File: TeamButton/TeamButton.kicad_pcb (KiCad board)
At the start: 2 copper layers, 79.9 x 70 mm, 5 parts, among them J1 RJ45, SW1 10T85 Microswitch, SW2 10T85 Microswitch

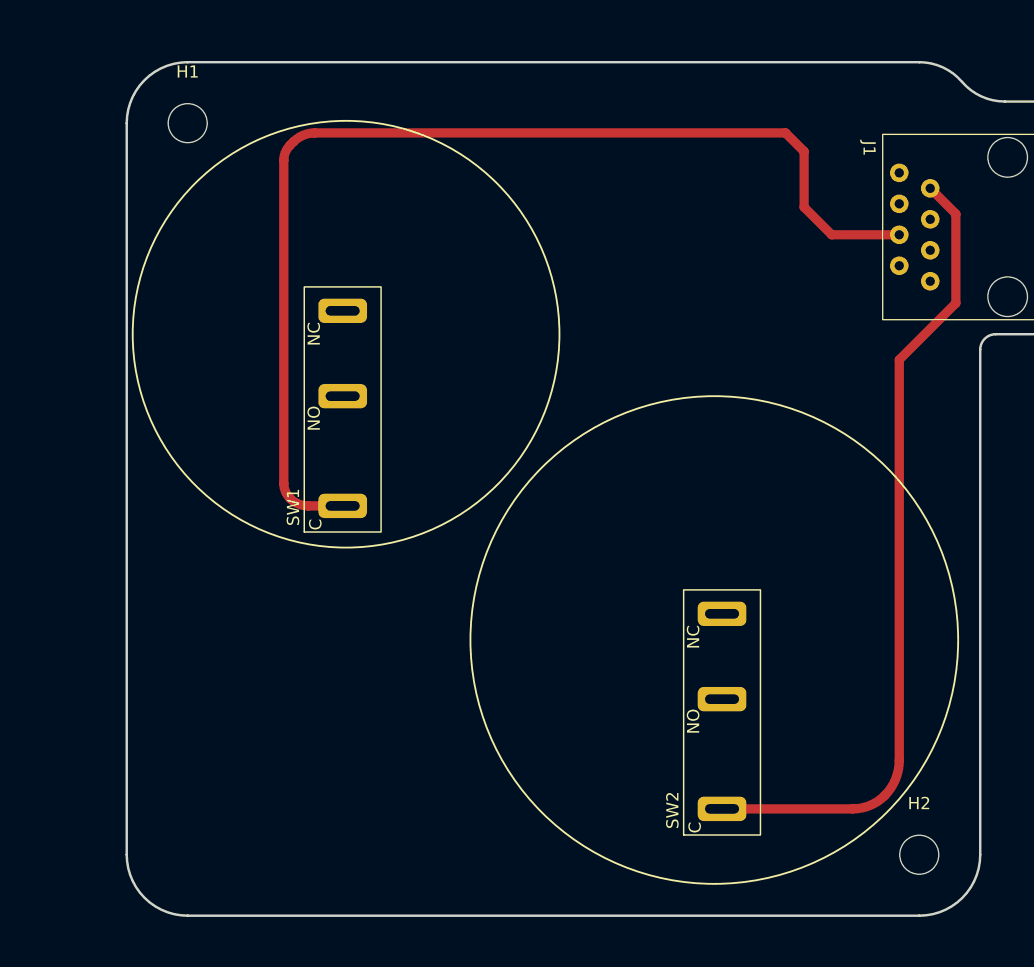
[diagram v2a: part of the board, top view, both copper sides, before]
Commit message: Added gay notations.
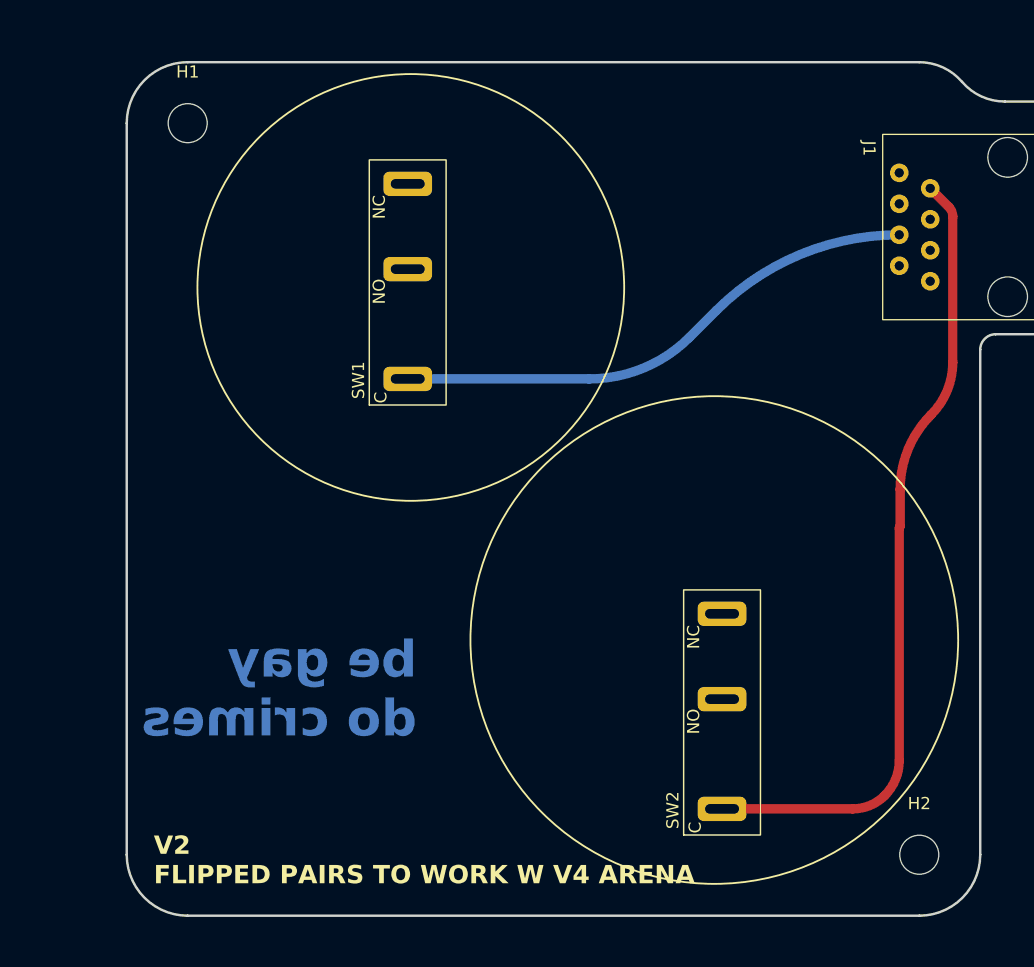
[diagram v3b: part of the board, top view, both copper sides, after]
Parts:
- moved SW1 11.7 mm to (94.9, 73.1)
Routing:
- net Net-(SW1-C): track 90.1 -> 43.6 mm
- net Net-(SW2-C): track 66.5 -> 65.5 mm
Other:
- board text added: "be gay do crimes"

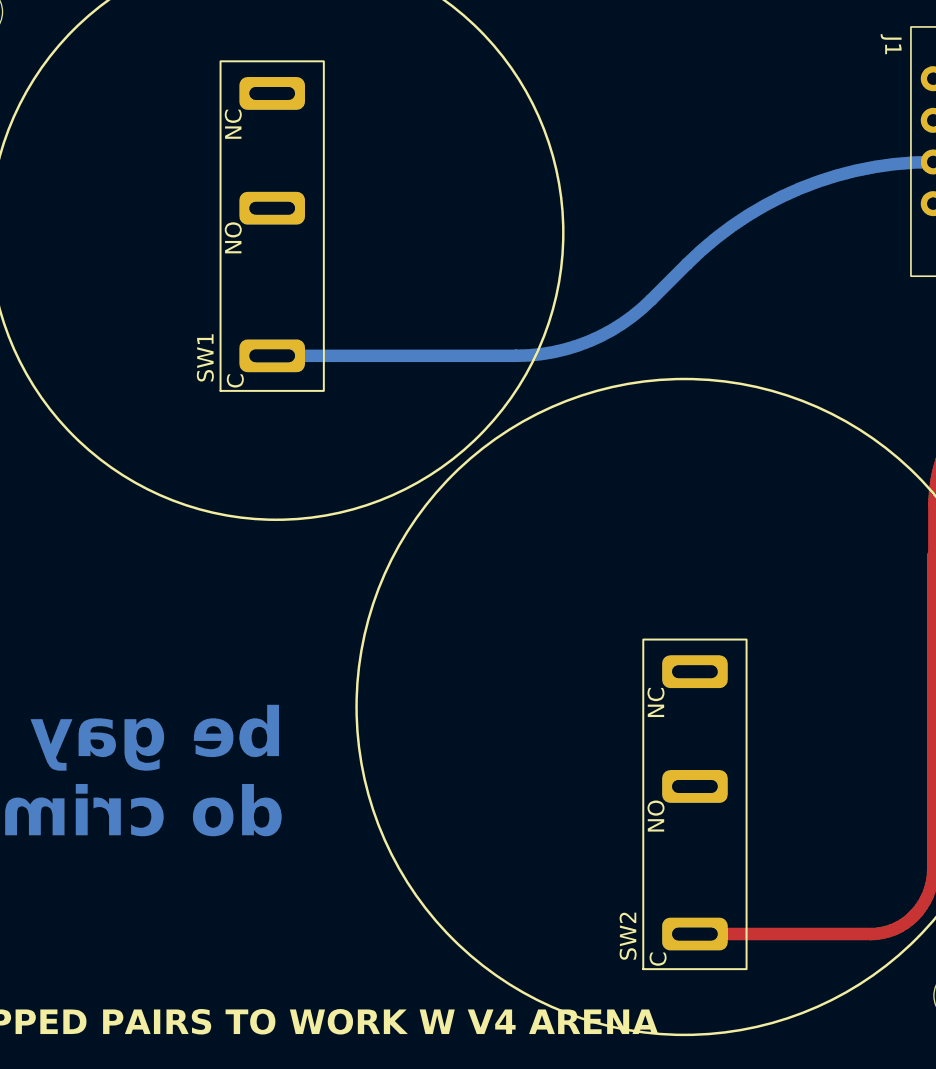
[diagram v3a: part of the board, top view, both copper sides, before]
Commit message: Added spacer mounting holes to board in case are needed.  Insert through back first.  Use smaller fasteners, etc.  Only one hole should be needed.
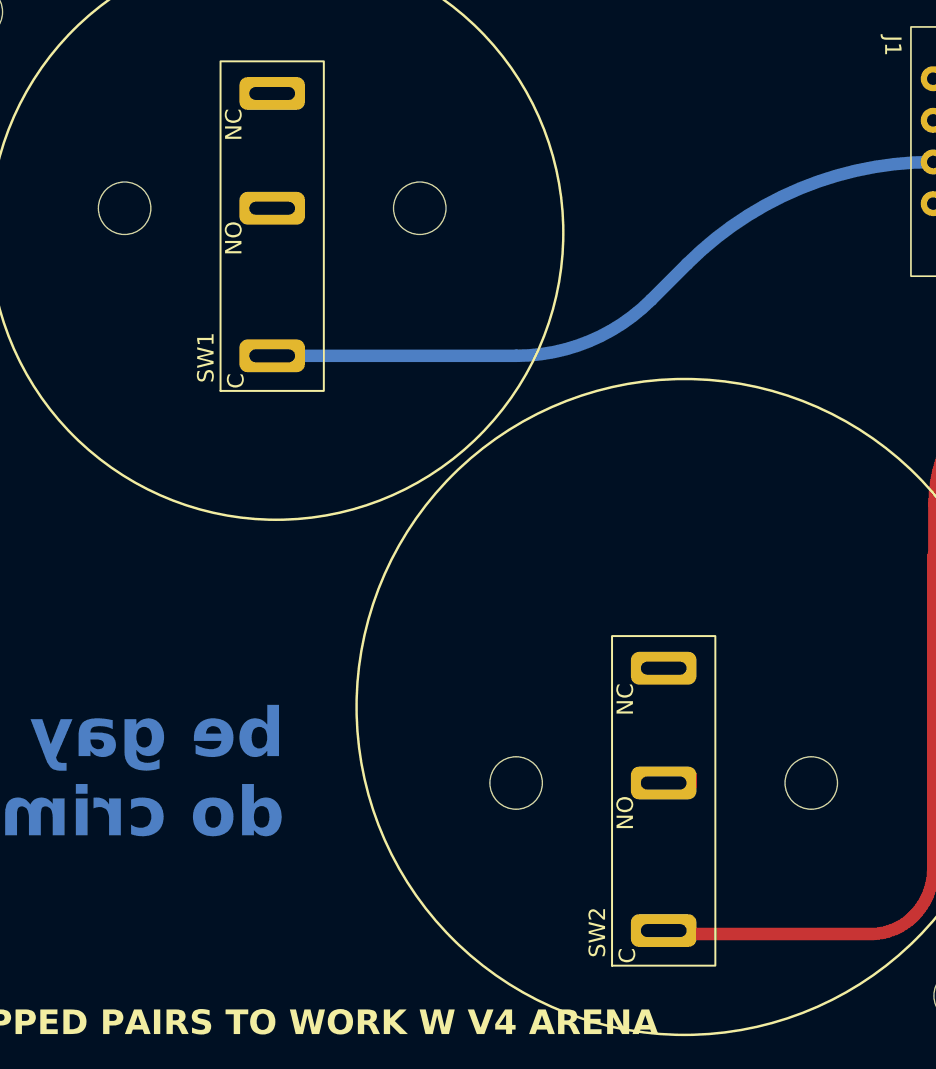
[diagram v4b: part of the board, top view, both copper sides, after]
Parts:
- SW1, SW2: footprint footprints:10T85 Microswitch -> footprints:10T85 Microswitch with M3 mounts
- moved SW1 11.6 mm to (98.0, 62.0)
- moved SW2 11.4 mm to (121.9, 97.0)
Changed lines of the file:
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@@
     (pad "" np_thru_hole circle (at 0 0) (size 3.2 3.2) (drill 3.2) (layers "*.Cu" "*.Mask"))
   )
-  (footprint "footprints:10T85 Microswitch" (layer "F.Cu")
-    (at 94.894 73.116 90)
+  (footprint "footprints:10T85 Microswitch with M3 mounts" (layer "F.Cu")
+    (at 98.044 61.976 90)
     (property "Sheetfile" "TeamButton.kicad_sch")
     (property "Sheetname" "")
@@
     (property "ki_keywords" "switch single-pole double-throw spdt ON-ON")
     (attr through_hole)
-    (fp_text reference "SW1" (at 2.032 -0.889 90 unlocked) (layer "F.SilkS")
+    (fp_text reference "SW1" (at -9.108 -4.039 90 unlocked) (layer "F.SilkS")
         (effects (font (size 1 1) (thickness 0.15)))
     )
-    (fp_text value "10T85 Microswitch" (at 7.366 7.747 90 unlocked) (layer "F.Fab")
+    (fp_text value "10T85 Microswitch" (at -3.774 4.597 90 unlocked) (layer "F.Fab")
         (effects (font (size 1 1) (thickness 0.15)))
     )
-    (fp_text user "NO" (at 8.255 1.397 90 unlocked) (layer "F.SilkS")
+    (fp_text user "NO" (at -2.885 -1.753 90 unlocked) (layer "F.SilkS")
         (effects (font (size 1 1) (thickness 0.15)) (justify left bottom))
     )
-    (fp_text user "C" (at 0.127 1.524 90 unlocked) (layer "F.SilkS")
+    (fp_text user "NC" (at 4.1 -1.753 90 unlocked) (layer "F.SilkS")
         (effects (font (size 1 1) (thickness 0.15)) (justify left bottom))
     )
-    (fp_text user "NC" (at 15.24 1.397 90 unlocked) (layer "F.SilkS")
+    (fp_text user "C" (at -11.013 -1.626 90 unlocked) (layer "F.SilkS")
         (effects (font (size 1 1) (thickness 0.15)) (justify left bottom))
     )
-    (fp_text user "${REFERENCE}" (at 5.715 9.525 90 unlocked) (layer "F.Fab")
+    (fp_text user "${REFERENCE}" (at -5.425 6.375 90 unlocked) (layer "F.Fab")
         (effects (font (size 1 1) (thickness 0.15)))
     )
-    (fp_rect (start 0 0) (end 20.1 6.3)
+    (fp_rect (start -11.14 -3.15) (end 8.96 3.15)
       (stroke (width 0.12) (type default)) (fill none) (layer "F.SilkS"))
-    (pad "1" thru_hole roundrect (at 2.14 3.15 180) (size 4 2) (drill oval 2.8 0.8) (layers "*.Cu" "*.Mask") (roundrect_rratio 0.25)
+    (fp_circle (center 0 -9) (end 3.2 -9)
+      (stroke (width 0.15) (type solid)) (fill none) (layer "Cmts.User"))
+    (fp_circle (center 0 9) (end 3.2 9)
+      (stroke (width 0.15) (type solid)) (fill none) (layer "Cmts.User"))
+    (fp_circle (center 0 -9) (end 3.45 -9)
+      (stroke (width 0.05) (type solid)) (fill none) (layer "F.CrtYd"))
+    (fp_circle (center 0 9) (end 3.45 9)
+      (stroke (width 0.05) (type solid)) (fill none) (layer "F.CrtYd"))
+    (pad "" np_thru_hole circle (at 0 -9 90) (size 3.2 3.2) (drill 3.2) (layers "F&B.Cu" "*.Mask"))
+    (pad "" np_thru_hole circle (at 0 9 90) (size 3.2 3.2) (drill 3.2) (layers "F&B.Cu" "*.Mask"))
+    (pad "1" thru_hole roundrect (at -9 0 180) (size 4 2) (drill oval 2.8 0.8) (layers "*.Cu" "*.Mask") (roundrect_rratio 0.25)
       (net 8 "Net-(SW1-C)") (pinfunction "C") (pintype "passive"))
-    (pad "2" thru_hole roundrect (at 18.14 3.15 180) (size 4 2) (drill oval 2.8 0.8) (layers "*.Cu" "*.Mask") (roundrect_rratio 0.25)
+    (pad "2" thru_hole roundrect (at 7 0 180) (size 4 2) (drill oval 2.8 0.8) (layers "*.Cu" "*.Mask") (roundrect_rratio 0.25)
       (net 9 "unconnected-(SW1-NC-Pad2)") (pinfunction "NC") (pintype "passive"))
-    (pad "3" thru_hole roundrect (at 11.14 3.15 180) (size 4 2) (drill oval 2.8 0.8) (layers "*.Cu" "*.Mask") (roundrect_rratio 0.25)
+    (pad "3" thru_hole roundrect (at 0 0 180) (size 4 2) (drill oval 2.8 0.8) (layers "*.Cu" "*.Mask") (roundrect_rratio 0.25)
       (net 1 "GND") (pinfunction "NO") (pintype "passive"))
   )
-  (footprint "footprints:10T85 Microswitch" (layer "F.Cu")
-    (at 120.675 108.38 90)
+  (footprint "footprints:10T85 Microswitch with M3 mounts" (layer "F.Cu")
+    (at 121.92 97.028 90)
     (property "Sheetfile" "TeamButton.kicad_sch")
     (property "Sheetname" "")
@@
     (property "ki_keywords" "switch single-pole double-throw spdt ON-ON")
     (attr through_hole)
-    (fp_text reference "SW2" (at 2.032 -0.889 90 unlocked) (layer "F.SilkS")
+    (fp_text reference "SW2" (at -9.108 -4.039 90 unlocked) (layer "F.SilkS")
         (effects (font (size 1 1) (thickness 0.15)))
     )
-    (fp_text value "10T85 Microswitch" (at 7.366 7.747 90 unlocked) (layer "F.Fab")
+    (fp_text value "10T85 Microswitch" (at -3.774 4.597 90 unlocked) (layer "F.Fab")
         (effects (font (size 1 1) (thickness 0.15)))
     )
-    (fp_text user "C" (at 0.127 1.524 90 unlocked) (layer "F.SilkS")
+    (fp_text user "C" (at -11.013 -1.626 90 unlocked) (layer "F.SilkS")
         (effects (font (size 1 1) (thickness 0.15)) (justify left bottom))
     )
-    (fp_text user "NC" (at 15.24 1.397 90 unlocked) (layer "F.SilkS")
+    (fp_text user "NC" (at 4.1 -1.753 90 unlocked) (layer "F.SilkS")
         (effects (font (size 1 1) (thickness 0.15)) (justify left bottom))
     )
-    (fp_text user "NO" (at 8.255 1.397 90 unlocked) (layer "F.SilkS")
+    (fp_text user "NO" (at -2.885 -1.753 90 unlocked) (layer "F.SilkS")
         (effects (font (size 1 1) (thickness 0.15)) (justify left bottom))
     )
-    (fp_text user "${REFERENCE}" (at 5.715 9.525 90 unlocked) (layer "F.Fab")
+    (fp_text user "${REFERENCE}" (at -5.425 6.375 90 unlocked) (layer "F.Fab")
         (effects (font (size 1 1) (thickness 0.15)))
     )
-    (fp_rect (start 0 0) (end 20.1 6.3)
+    (fp_rect (start -11.14 -3.15) (end 8.96 3.15)
       (stroke (width 0.12) (type default)) (fill none) (layer "F.SilkS"))
-    (pad "1" thru_hole roundrect (at 2.14 3.15 180) (size 4 2) (drill oval 2.8 0.8) (layers "*.Cu" "*.Mask") (roundrect_rratio 0.25)
+    (fp_circle (center 0 -9) (end 3.2 -9)
+      (stroke (width 0.15) (type solid)) (fill none) (layer "Cmts.User"))
+    (fp_circle (center 0 9) (end 3.2 9)
+      (stroke (width 0.15) (type solid)) (fill none) (layer "Cmts.User"))
+    (fp_circle (center 0 -9) (end 3.45 -9)
+      (stroke (width 0.05) (type solid)) (fill none) (layer "F.CrtYd"))
+    (fp_circle (center 0 9) (end 3.45 9)
+      (stroke (width 0.05) (type solid)) (fill none) (layer "F.CrtYd"))
+    (pad "" np_thru_hole circle (at 0 -9 90) (size 3.2 3.2) (drill 3.2) (layers "F&B.Cu" "*.Mask"))
+    (pad "" np_thru_hole circle (at 0 9 90) (size 3.2 3.2) (drill 3.2) (layers "F&B.Cu" "*.Mask"))
+    (pad "1" thru_hole roundrect (at -9 0 180) (size 4 2) (drill oval 2.8 0.8) (layers "*.Cu" "*.Mask") (roundrect_rratio 0.25)
       (net 6 "Net-(SW2-C)") (pinfunction "C") (pintype "passive"))
-    (pad "2" thru_hole roundrect (at 18.14 3.15 180) (size 4 2) (drill oval 2.8 0.8) (layers "*.Cu" "*.Mask") (roundrect_rratio 0.25)
+    (pad "2" thru_hole roundrect (at 7 0 180) (size 4 2) (drill oval 2.8 0.8) (layers "*.Cu" "*.Mask") (roundrect_rratio 0.25)
       (net 10 "unconnected-(SW2-NC-Pad2)") (pinfunction "NC") (pintype "passive"))
-    (pad "3" thru_hole roundrect (at 11.14 3.15 180) (size 4 2) (drill oval 2.8 0.8) (layers "*.Cu" "*.Mask") (roundrect_rratio 0.25)
+    (pad "3" thru_hole roundrect (at 0 0 180) (size 4 2) (drill oval 2.8 0.8) (layers "*.Cu" "*.Mask") (roundrect_rratio 0.25)
       (net 1 "GND") (pinfunction "NO") (pintype "passive"))
   )
